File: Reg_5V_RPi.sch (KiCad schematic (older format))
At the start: 0 parts

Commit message: cleanup
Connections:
- net labels added: EN, VIN, VOUT
- net labels removed: Enable, VIN_MS, VOUT_MS
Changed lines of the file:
@@
 LIBS:valves
 LIBS:hedgehog_symbols
+LIBS:switches
 LIBS:Hedgehog-cache
-EELAYER 25 0
+EELAYER 26 0
 EELAYER END
 $Descr A4 11693 8268
 encoding utf-8
-Sheet 2 8
+Sheet 3 8
 Title ""
 Date ""
@@
 Comment4 ""
 $EndDescr
-Text HLabel 2250 2550 0    60   Input ~ 0
-VIN_MS
-Text HLabel 6300 2600 2    60   Output ~ 0
-VOUT_MS
+Text HLabel 2050 3050 0    60   Input ~ 0
+VIN
+Text HLabel 1600 2700 0    60   Input ~ 0
+EN
+Text HLabel 5900 3050 2    60   Input ~ 0
+VOUT
 Wire Wire Line
-	2250 2550 3200 2550
+	1600 2700 3100 2700
 Wire Wire Line
-	6300 2600 5800 2600
-Text HLabel 2250 2050 0    60   Input ~ 0
-Enable
+	2050 3050 3200 3050
 Wire Wire Line
-	2250 2050 3200 2050
+	5900 3050 5100 3050
 $EndSCHEMATC

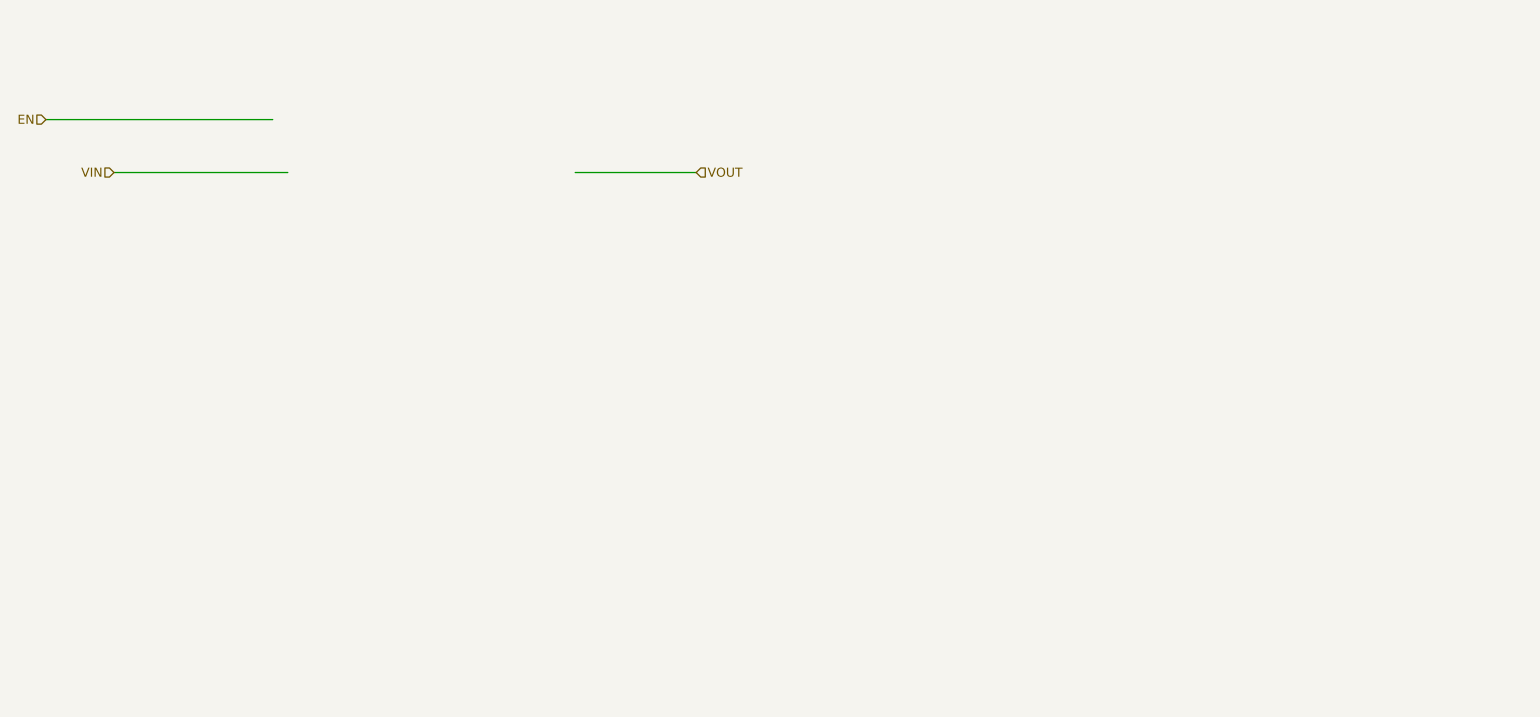
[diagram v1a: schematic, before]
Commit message: added RPi Regulator added ref.des.-prefixes to all schematic sheets
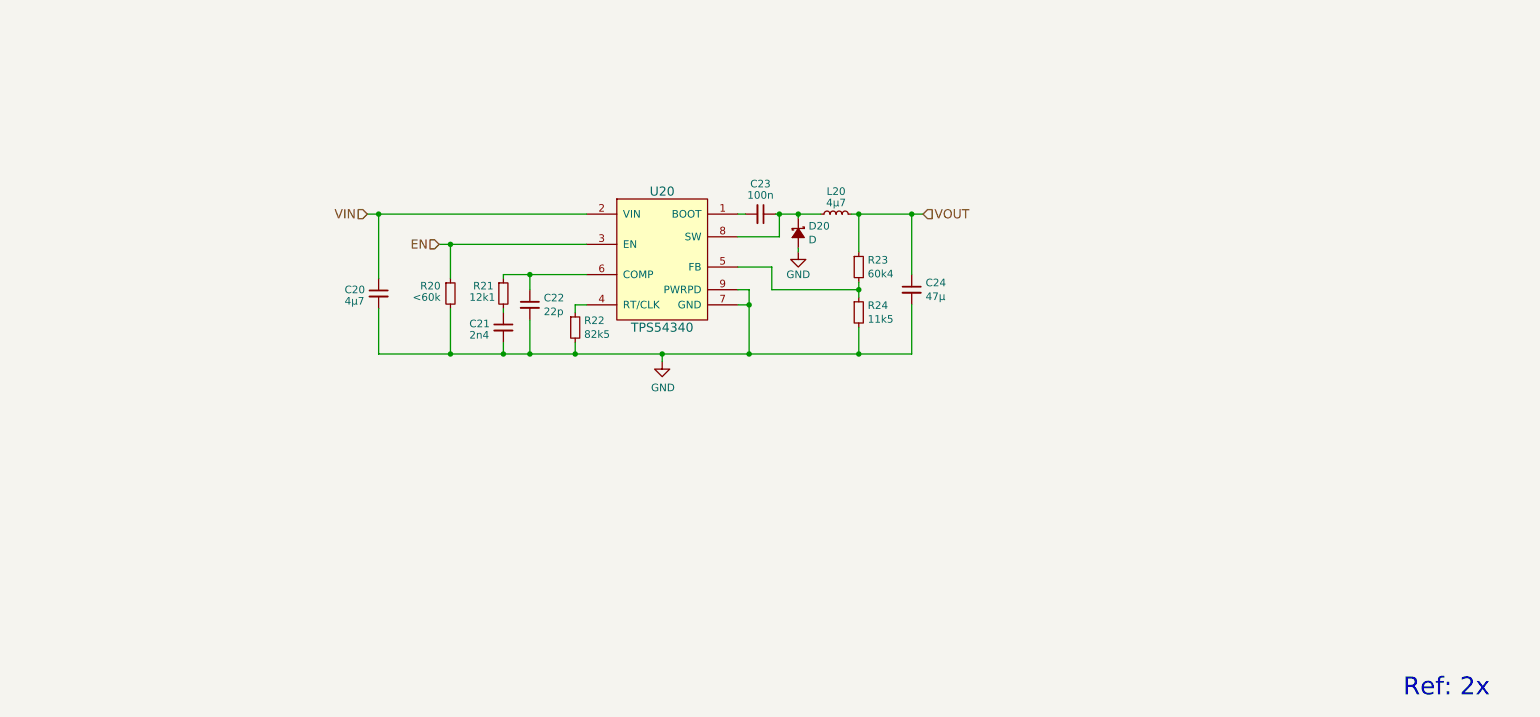
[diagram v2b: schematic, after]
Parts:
- added C20: 4µ7, symbol C_Small
- added C21: 2n4, symbol C_Small
- added C22: 22p, symbol C_Small
- added C23: 100n, symbol C_Small
- added C24: 47µ, symbol C_Small
- added D20: D, symbol D_Schottky_Small_ALT
- added L20: 4µ7, symbol L_Small
- added R20: <60k, symbol R_Small
- added R21: 12k1, symbol R_Small
- added R22: 82k5, symbol R_Small
- added R23: 60k4, symbol R_Small
- added R24: 11k5, symbol R_Small
- added U20: TPS54340, symbol TPS54340
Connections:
- net labels added: GND
- wire segments 3 -> 51
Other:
- note added: "Ref: 2x"

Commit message: added 3v3 regulator
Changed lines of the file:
@@
 	5100 3925 5100 3975
 Wire Wire Line
-	4625 3725 4800 3725
-Wire Wire Line
-	4800 3725 5175 3725
+	4625 3725 5175 3725
 Wire Wire Line
 	4625 3725 4625 3750
@@
 Connection ~ 4800 3725
 Wire Wire Line
-	4200 3525 4275 3525
-Wire Wire Line
-	4275 3525 5175 3525
+	4200 3525 5175 3525
 Wire Wire Line
 	4275 3750 4275 3525
 Connection ~ 4275 3525
 Wire Wire Line
-	3725 3325 3800 3325
-Wire Wire Line
-	3800 3325 5175 3325
+	3725 3325 5175 3325
 Wire Wire Line
 	3800 3325 3800 3750
@@
 	6175 3325 6225 3325
 Wire Wire Line
-	6425 3325 6450 3325
-Wire Wire Line
-	6450 3325 6575 3325
-Wire Wire Line
-	6575 3325 6725 3325
+	6425 3325 6725 3325
 Wire Wire Line
 	6450 3325 6450 3475
@@
 Connection ~ 6575 3325
 Wire Wire Line
-	6925 3325 6975 3325
-Wire Wire Line
-	6975 3325 7325 3325
-Wire Wire Line
-	7325 3325 7400 3325
+	6925 3325 7400 3325
 Wire Wire Line
 	6975 3325 6975 3575
@@
 Connection ~ 7325 3325
 Wire Wire Line
-	6975 3775 6975 3825
-Wire Wire Line
-	6975 3825 6975 3875
+	6975 3775 6975 3875
 $Comp
 L GND #PWR?
@@
 Connection ~ 6975 3825
 Wire Wire Line
-	3800 4250 4275 4250
-Wire Wire Line
-	4275 4250 4625 4250
-Wire Wire Line
-	4625 4250 4800 4250
-Wire Wire Line
-	4800 4250 5100 4250
-Wire Wire Line
-	5100 4250 5675 4250
-Wire Wire Line
-	5675 4250 6250 4250
-Wire Wire Line
-	6250 4250 6975 4250
-Wire Wire Line
-	6975 4250 7325 4250
+	3800 4250 7325 4250
 Wire Wire Line
 	3800 4250 3800 3950
@@
 	6175 3825 6250 3825
 Wire Wire Line
-	6250 3825 6250 3925
-Wire Wire Line
-	6250 3925 6250 4250
+	6250 3825 6250 4250
 Connection ~ 6250 4250
 Wire Wire Line

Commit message: added HSOP-8,LSON-22,Mini-F3-B,MSOP-10,SOD323F Footprint finished package assignment (without inductors )
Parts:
- C20, C21, C22: footprint (none) -> Capacitors_SMD:C_0603_HandSoldering
- C23: footprint (none) -> Capacitors_SMD:C_0402
- C24: footprint (none) -> Capacitors_SMD:C_1206_HandSoldering
- D20: footprint (none) -> Diodes_SMD:D_SMC_Handsoldering
- R20, R21, R22, R23, R24: footprint (none) -> Resistors_SMD:R_0402
- U20: footprint (none) -> hedgehog_footprints:HSOP-8
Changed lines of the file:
@@
 F 0 "U20" H 5675 4075 60  0000 C CNN
 F 1 "TPS54340" H 5675 3175 60  0000 C CNN
-F 2 "" H 5325 2825 60  0001 C CNN
+F 2 "hedgehog_footprints:HSOP-8" H 5325 2825 60  0001 C CNN
 F 3 "" H 5325 2825 60  0001 C CNN
 	1    5675 3625
@@
 F 0 "C20" H 3575 3875 50  0000 L CNN
 F 1 "4µ7" H 3575 3800 50  0000 L CNN
-F 2 "" H 3800 3850 50  0001 C CNN
+F 2 "Capacitors_SMD:C_0603_HandSoldering" H 3800 3850 50  0001 C CNN
 F 3 "" H 3800 3850 50  0001 C CNN
 	1    3800 3850
@@
 F 0 "C21" H 4400 4100 50  0000 L CNN
 F 1 "2n4" H 4400 4025 50  0000 L CNN
-F 2 "" H 4625 4075 50  0001 C CNN
+F 2 "Capacitors_SMD:C_0603_HandSoldering" H 4625 4075 50  0001 C CNN
 F 3 "" H 4625 4075 50  0001 C CNN
 	1    4625 4075
@@
 F 0 "C22" H 4892 3971 50  0000 L CNN
 F 1 "22p" H 4892 3880 50  0000 L CNN
-F 2 "" H 4800 3925 50  0001 C CNN
+F 2 "Capacitors_SMD:C_0603_HandSoldering" H 4800 3925 50  0001 C CNN
 F 3 "" H 4800 3925 50  0001 C CNN
 	1    4800 3925
@@
 F 0 "C23" V 6125 3325 50  0000 C CNN
 F 1 "100n" V 6200 3325 50  0000 C CNN
-F 2 "" H 6325 3325 50  0001 C CNN
+F 2 "Capacitors_SMD:C_0402" H 6325 3325 50  0001 C CNN
 F 3 "" H 6325 3325 50  0001 C CNN
 	1    6325 3325
@@
 F 0 "C24" H 7417 3871 50  0000 L CNN
 F 1 "47µ" H 7417 3780 50  0000 L CNN
-F 2 "" H 7325 3825 50  0001 C CNN
+F 2 "Capacitors_SMD:C_1206_HandSoldering" H 7325 3825 50  0001 C CNN
 F 3 "" H 7325 3825 50  0001 C CNN
 	1    7325 3825
@@
 F 0 "R21" H 4425 3900 50  0000 L CNN
 F 1 "12k1" H 4400 3825 50  0000 L CNN
-F 2 "" H 4625 3850 50  0001 C CNN
+F 2 "Resistors_SMD:R_0402" H 4625 3850 50  0001 C CNN
 F 3 "" H 4625 3850 50  0001 C CNN
 	1    4625 3850
@@
 F 0 "R22" H 5159 4121 50  0000 L CNN
 F 1 "82k5" H 5159 4030 50  0000 L CNN
-F 2 "" H 5100 4075 50  0001 C CNN
+F 2 "Resistors_SMD:R_0402" H 5100 4075 50  0001 C CNN
 F 3 "" H 5100 4075 50  0001 C CNN
 	1    5100 4075
@@
 F 0 "R23" H 7034 3721 50  0000 L CNN
 F 1 "60k4" H 7034 3630 50  0000 L CNN
-F 2 "" H 6975 3675 50  0001 C CNN
+F 2 "Resistors_SMD:R_0402" H 6975 3675 50  0001 C CNN
 F 3 "" H 6975 3675 50  0001 C CNN
 	1    6975 3675
@@
 F 0 "R24" H 7034 4021 50  0000 L CNN
 F 1 "11k5" H 7034 3930 50  0000 L CNN
-F 2 "" H 6975 3975 50  0001 C CNN
+F 2 "Resistors_SMD:R_0402" H 6975 3975 50  0001 C CNN
 F 3 "" H 6975 3975 50  0001 C CNN
 	1    6975 3975
@@
 F 0 "D20" V 6529 3518 50  0000 L CNN
 F 1 "D" V 6620 3518 50  0000 L CNN
-F 2 "" V 6575 3450 50  0001 C CNN
+F 2 "Diodes_SMD:D_SMC_Handsoldering" V 6575 3450 50  0001 C CNN
 F 3 "" V 6575 3450 50  0001 C CNN
 	1    6575 3450
@@
 F 0 "R20" H 4075 3900 50  0000 L CNN
 F 1 "<60k" H 4025 3825 50  0000 L CNN
-F 2 "" H 4275 3850 50  0001 C CNN
+F 2 "Resistors_SMD:R_0402" H 4275 3850 50  0001 C CNN
 F 3 "" H 4275 3850 50  0001 C CNN
 	1    4275 3850

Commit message: fixed some footprints, should now be correct and complete
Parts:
- C20, C21, C22: footprint Capacitors_SMD:C_0603_HandSoldering -> Capacitors_SMD:C_0603
- C23: footprint Capacitors_SMD:C_0402 -> Capacitors_SMD:C_0603
- C24: footprint Capacitors_SMD:C_1206_HandSoldering -> Capacitors_SMD:C_1206
- D20: footprint Diodes_SMD:D_SMC_Handsoldering -> hedgehog_footprints:SMC
- L20: footprint (none) -> hedgehog_footprints:VLP8040
- R20, R21, R22, R23, R24: footprint Resistors_SMD:R_0402 -> Resistors_SMD:R_0603
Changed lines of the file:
@@
 LIBS:switches
 LIBS:Hedgehog-cache
-EELAYER 25 0
+EELAYER 26 0
 EELAYER END
 $Descr A4 11693 8268
@@
 F 0 "C20" H 3575 3875 50  0000 L CNN
 F 1 "4µ7" H 3575 3800 50  0000 L CNN
-F 2 "Capacitors_SMD:C_0603_HandSoldering" H 3800 3850 50  0001 C CNN
+F 2 "Capacitors_SMD:C_0603" H 3800 3850 50  0001 C CNN
 F 3 "" H 3800 3850 50  0001 C CNN
 	1    3800 3850
@@
 F 0 "C21" H 4400 4100 50  0000 L CNN
 F 1 "2n4" H 4400 4025 50  0000 L CNN
-F 2 "Capacitors_SMD:C_0603_HandSoldering" H 4625 4075 50  0001 C CNN
+F 2 "Capacitors_SMD:C_0603" H 4625 4075 50  0001 C CNN
 F 3 "" H 4625 4075 50  0001 C CNN
 	1    4625 4075
@@
 F 0 "C22" H 4892 3971 50  0000 L CNN
 F 1 "22p" H 4892 3880 50  0000 L CNN
-F 2 "Capacitors_SMD:C_0603_HandSoldering" H 4800 3925 50  0001 C CNN
+F 2 "Capacitors_SMD:C_0603" H 4800 3925 50  0001 C CNN
 F 3 "" H 4800 3925 50  0001 C CNN
 	1    4800 3925
@@
 F 0 "C23" V 6125 3325 50  0000 C CNN
 F 1 "100n" V 6200 3325 50  0000 C CNN
-F 2 "Capacitors_SMD:C_0402" H 6325 3325 50  0001 C CNN
+F 2 "Capacitors_SMD:C_0603" H 6325 3325 50  0001 C CNN
 F 3 "" H 6325 3325 50  0001 C CNN
 	1    6325 3325
@@
 F 0 "C24" H 7417 3871 50  0000 L CNN
 F 1 "47µ" H 7417 3780 50  0000 L CNN
-F 2 "Capacitors_SMD:C_1206_HandSoldering" H 7325 3825 50  0001 C CNN
+F 2 "Capacitors_SMD:C_1206" H 7325 3825 50  0001 C CNN
 F 3 "" H 7325 3825 50  0001 C CNN
 	1    7325 3825
@@
 F 0 "R21" H 4425 3900 50  0000 L CNN
 F 1 "12k1" H 4400 3825 50  0000 L CNN
-F 2 "Resistors_SMD:R_0402" H 4625 3850 50  0001 C CNN
+F 2 "Resistors_SMD:R_0603" H 4625 3850 50  0001 C CNN
 F 3 "" H 4625 3850 50  0001 C CNN
 	1    4625 3850
@@
 F 0 "R22" H 5159 4121 50  0000 L CNN
 F 1 "82k5" H 5159 4030 50  0000 L CNN
-F 2 "Resistors_SMD:R_0402" H 5100 4075 50  0001 C CNN
+F 2 "Resistors_SMD:R_0603" H 5100 4075 50  0001 C CNN
 F 3 "" H 5100 4075 50  0001 C CNN
 	1    5100 4075
@@
 F 0 "R23" H 7034 3721 50  0000 L CNN
 F 1 "60k4" H 7034 3630 50  0000 L CNN
-F 2 "Resistors_SMD:R_0402" H 6975 3675 50  0001 C CNN
+F 2 "Resistors_SMD:R_0603" H 6975 3675 50  0001 C CNN
 F 3 "" H 6975 3675 50  0001 C CNN
 	1    6975 3675
@@
 F 0 "R24" H 7034 4021 50  0000 L CNN
 F 1 "11k5" H 7034 3930 50  0000 L CNN
-F 2 "Resistors_SMD:R_0402" H 6975 3975 50  0001 C CNN
+F 2 "Resistors_SMD:R_0603" H 6975 3975 50  0001 C CNN
 F 3 "" H 6975 3975 50  0001 C CNN
 	1    6975 3975
@@
 F 0 "L20" V 6975 3325 50  0000 C CNN
 F 1 "4µ7" V 6900 3325 50  0000 C CNN
-F 2 "" H 6825 3325 50  0001 C CNN
+F 2 "hedgehog_footprints:VLP8040" H 6825 3325 50  0001 C CNN
 F 3 "" H 6825 3325 50  0001 C CNN
 	1    6825 3325
@@
 F 0 "D20" V 6529 3518 50  0000 L CNN
 F 1 "D" V 6620 3518 50  0000 L CNN
-F 2 "Diodes_SMD:D_SMC_Handsoldering" V 6575 3450 50  0001 C CNN
+F 2 "hedgehog_footprints:SMC" V 6575 3450 50  0001 C CNN
 F 3 "" V 6575 3450 50  0001 C CNN
 	1    6575 3450
@@
 F 0 "R20" H 4075 3900 50  0000 L CNN
 F 1 "<60k" H 4025 3825 50  0000 L CNN
-F 2 "Resistors_SMD:R_0402" H 4275 3850 50  0001 C CNN
+F 2 "Resistors_SMD:R_0603" H 4275 3850 50  0001 C CNN
 F 3 "" H 4275 3850 50  0001 C CNN
 	1    4275 3850
